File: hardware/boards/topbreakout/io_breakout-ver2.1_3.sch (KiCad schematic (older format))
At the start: 8 parts, among them J1 WURTH_ELECTRONICS_61400413321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, J2 MOLEX_52892-3033MOLEX_52892-3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, J3 USB-A-S-X-X-VT, J5 Conn_01x40

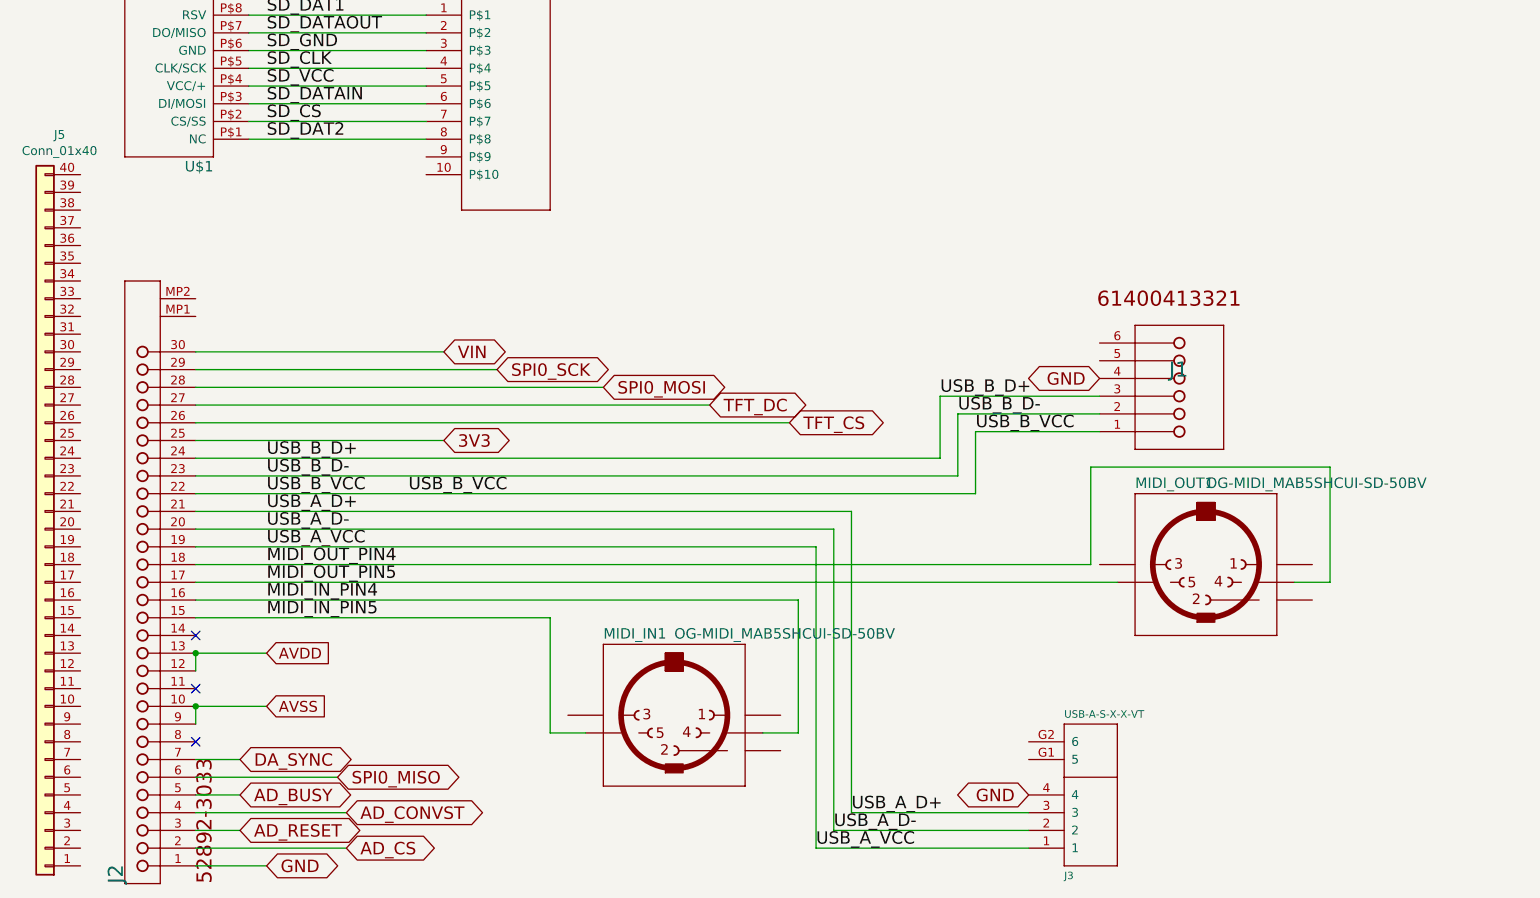
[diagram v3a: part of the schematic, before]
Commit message: moved midi circuit to breakout board
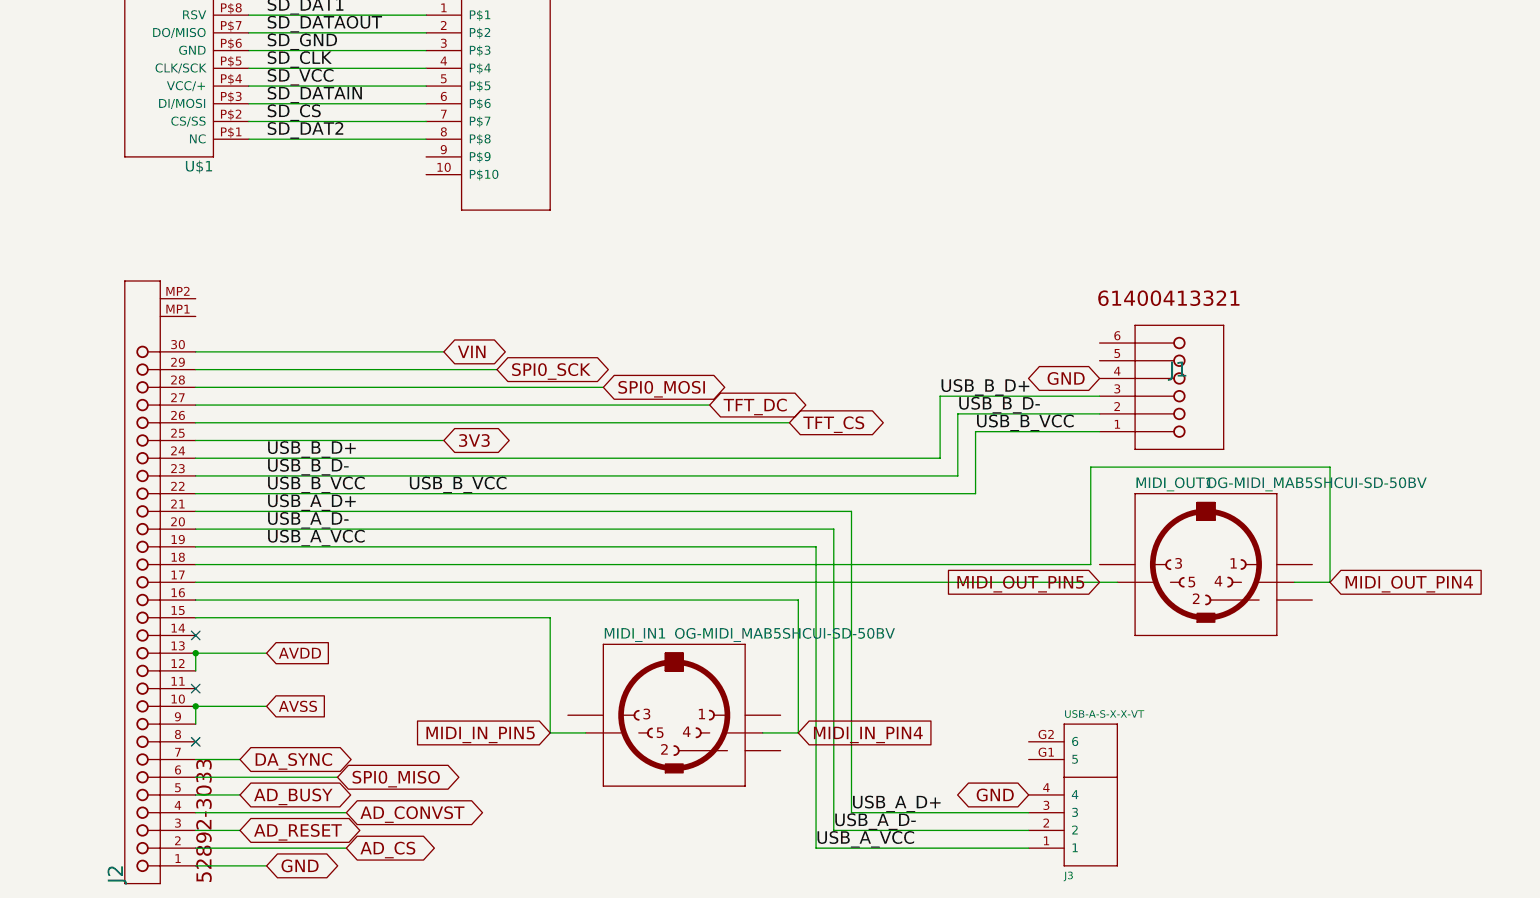
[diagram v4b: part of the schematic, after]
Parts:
- removed J5: Conn_01x40, Connectors_TE-Connectivity:TE_2-84953-7_1x27_P1.0mm_Horizontal, symbol Connector_Generic:Conn_01x40
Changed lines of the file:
@@
 $Descr User 14469 9224
 encoding utf-8
-Sheet 4 7
+Sheet 4 8
 Title ""
 Date ""
@@
 Wire Wire Line
 	1400 4600 3400 4600
-Text Label 1800 4600 0    70   ~ 0
-MIDI_IN_PIN5
-Text Label 1800 4500 0    70   ~ 0
-MIDI_IN_PIN4
-Text Label 1800 4400 0    70   ~ 0
-MIDI_OUT_PIN5
 Wire Wire Line
 	1400 4300 6450 4300
@@
 Wire Wire Line
 	6450 3750 7800 3750
-Text Label 1800 4300 0    70   ~ 0
-MIDI_OUT_PIN4
 Wire Wire Line
 	1400 4100 5000 4100
@@
 Text GLabel 1800 5100 2    61   Input ~ 0
 AVSS
-$Comp
-L Connector_Generic:Conn_01x40 J5
-U 1 1 5D8E7BFB
-P 550 4100
-F 0 "J5" H 468 1875 50  0000 C CNN
-F 1 "Conn_01x40" H 468 1966 50  0000 C CNN
-F 2 "Connectors_TE-Connectivity:TE_2-84953-7_1x27_P1.0mm_Horizontal" H 550 4100 50  0001 C CNN
-F 3 "~" H 550 4100 50  0001 C CNN
-	1    550  4100
-	-1   0    0    1
-$EndComp
+Text GLabel 7800 4400 2    70   Input ~ 0
+MIDI_OUT_PIN4
+Text GLabel 6500 4400 0    70   Input ~ 0
+MIDI_OUT_PIN5
+Text GLabel 4800 5250 2    70   Input ~ 0
+MIDI_IN_PIN4
+Text GLabel 3400 5250 0    70   Input ~ 0
+MIDI_IN_PIN5
 $EndSCHEMATC

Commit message: neaten up
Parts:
- removed MIDI_IN, MIDI_OUT: OG-MIDI_MAB5SHCUI-SD-50BV, topbreakout:OG-MIDI_SD-50BV, symbol TopBreakout-eagle-import:OG-MIDI_MAB5SHCUI-SD-50BV
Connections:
- net MIDI_IN_PIN4: no longer names the net of J2.16
- net MIDI_IN_PIN5: no longer names the net of J2.15
- net MIDI_OUT_PIN4 renamed MIDI_RX
- net MIDI_OUT_PIN5 renamed MIDI_TX
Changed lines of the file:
@@
 VIN
-Wire Wire Line
-	1400 4600 3400 4600
-Wire Wire Line
-	1400 4300 6450 4300
-Wire Wire Line
-	6450 4300 6450 3750
-Wire Wire Line
-	6450 3750 7800 3750
 Wire Wire Line
 	1400 4100 5000 4100
@@
 $EndComp
 $Comp
-L TopBreakout-eagle-import:OG-MIDI_MAB5SHCUI-SD-50BV MIDI_OUT
-U 1 1 74EA5AF5
-P 7100 4300
-AR Path="/74EA5AF5" Ref="MIDI_OUT"  Part="1"
-AR Path="/5D7F42FA/74EA5AF5" Ref="MIDI_OUT1"  Part="1"
-F 0 "MIDI_OUT1" H 6700 4725 59  0000 L BNN
-F 1 "OG-MIDI_MAB5SHCUI-SD-50BV" H 7100 4725 59  0000 L BNN
-F 2 "topbreakout:OG-MIDI_SD-50BV" H 7100 4300 50  0001 C CNN
-F 3 "" H 7100 4300 50  0001 C CNN
-	1    7100 4300
-	1    0    0    -1
-$EndComp
-$Comp
 L TopBreakout-eagle-import:MOLEX_52892-3033MOLEX_52892-3033_0_0 J2
 U 1 1 F1780596
@@
 $EndComp
 Wire Wire Line
-	3400 4600 3400 5250
-Wire Wire Line
 	6100 5900 4900 5900
-$Comp
-L TopBreakout-eagle-import:OG-MIDI_MAB5SHCUI-SD-50BV MIDI_IN
-U 1 1 1C421DBC
-P 4100 5150
-AR Path="/1C421DBC" Ref="MIDI_IN"  Part="1"
-AR Path="/5D7F42FA/1C421DBC" Ref="MIDI_IN1"  Part="1"
-F 0 "MIDI_IN1" H 3700 5575 59  0000 L BNN
-F 1 "OG-MIDI_MAB5SHCUI-SD-50BV" H 4100 5575 59  0000 L BNN
-F 2 "topbreakout:OG-MIDI_SD-50BV" H 4100 5150 50  0001 C CNN
-F 3 "" H 4100 5150 50  0001 C CNN
-	1    4100 5150
-	1    0    0    -1
-$EndComp
-Wire Wire Line
-	3400 5250 3600 5250
-Wire Wire Line
-	1400 4500 4800 4500
-Wire Wire Line
-	4600 5250 4800 5250
-Wire Wire Line
-	4800 5250 4800 4500
-Wire Wire Line
-	7600 4400 7800 4400
-Wire Wire Line
-	7800 4400 7800 3750
-Wire Wire Line
-	1400 4400 6600 4400
 Wire Wire Line
 	5100 5700 6100 5700
@@
 Text GLabel 1800 5100 2    61   Input ~ 0
 AVSS
-Text GLabel 7800 4400 2    70   Input ~ 0
-MIDI_OUT_PIN4
-Text GLabel 6500 4400 0    70   Input ~ 0
-MIDI_OUT_PIN5
-Text GLabel 4800 5250 2    70   Input ~ 0
-MIDI_IN_PIN4
-Text GLabel 3400 5250 0    70   Input ~ 0
-MIDI_IN_PIN5
+Text GLabel 1400 4300 2    59   Input ~ 0
+MIDI_RX
+Text GLabel 1400 4400 2    59   Input ~ 0
+MIDI_TX
 $EndSCHEMATC

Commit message: refactor
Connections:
- net AVDD: now also J2.10, J2.11; no longer J2.12, J2.13
- net AVSS: now also J2.8; no longer J2.10
- net GATE_2: now reaches J2.14
- net GATE_1: now reaches J2.15
- new net GATE_3: J2.13
- new net GATE_4: J2.12
- no-connect marks 3 -> 0
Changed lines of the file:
@@
-$EndComp
-$Comp
-L TopBreakout-eagle-import:MOLEX_52892-3033MOLEX_52892-3033_0_0 J2
-U 1 1 F1780596
-P 800 6100
-AR Path="/F1780596" Ref="J2"  Part="1"
-AR Path="/5D7F42FA/F1780596" Ref="J2"  Part="1"
-F 0 "J2" H 800 6000 85  0000 L TNN
-F 1 "MOLEX_52892-3033MOLEX_52892-3033_0_0" H 800 6100 50  0001 C CNN
-F 2 "topbreakout:MOLEX_52892-3033_0" H 800 6100 50  0001 C CNN
-F 3 "" H 800 6100 50  0001 C CNN
-	1    800  6100
-	0    -1   -1   0
 $EndComp
 $Comp
@@
 Wire Wire Line
 	5000 5800 6100 5800
-Wire Wire Line
-	1400 5200 1400 5100
-Wire Wire Line
-	1400 4900 1400 4800
-Wire Wire Line
-	1400 4800 1800 4800
-Connection ~ 1400 4800
-Wire Wire Line
-	1400 5100 1800 5100
-Connection ~ 1400 5100
-NoConn ~ 1400 5300
-NoConn ~ 1400 5000
-NoConn ~ 1400 4700
-Text GLabel 1800 4800 2    61   Input ~ 0
+Text GLabel 1800 5100 2    61   Input ~ 0
 AVDD
-Text GLabel 1800 5100 2    61   Input ~ 0
+Text GLabel 1800 5200 2    61   Input ~ 0
 AVSS
 Text GLabel 1400 4300 2    59   Input ~ 0
@@
 Text GLabel 1400 4400 2    59   Input ~ 0
 MIDI_TX
+$Comp
+L TopBreakout-eagle-import:MOLEX_52892-3033MOLEX_52892-3033_0_0 J2
+U 1 1 F1780596
+P 800 6100
+AR Path="/F1780596" Ref="J2"  Part="1"
+AR Path="/5D7F42FA/F1780596" Ref="J2"  Part="1"
+F 0 "J2" H 800 6000 85  0000 L TNN
+F 1 "MOLEX_52892-3033MOLEX_52892-3033_0_0" H 800 6100 50  0001 C CNN
+F 2 "topbreakout:MOLEX_52892-3033_0" H 800 6100 50  0001 C CNN
+F 3 "" H 800 6100 50  0001 C CNN
+	1    800  6100
+	0    -1   -1   0
+$EndComp
+Wire Wire Line
+	1400 5300 1400 5200
+Connection ~ 1400 5200
+Wire Wire Line
+	1400 5200 1800 5200
+Wire Wire Line
+	1800 5100 1400 5100
+Wire Wire Line
+	1400 5000 1400 5100
+Connection ~ 1400 5100
+Wire Wire Line
+	1400 4900 1600 4900
+Wire Wire Line
+	1400 4800 1600 4800
+Wire Wire Line
+	1400 4700 1600 4700
+Wire Wire Line
+	1400 4600 1600 4600
+Text GLabel 1600 4600 2    59   Input ~ 0
+GATE_1
+Text GLabel 1600 4700 2    59   Input ~ 0
+GATE_2
+Text GLabel 1600 4800 2    59   Input ~ 0
+GATE_3
+Text GLabel 1600 4900 2    59   Input ~ 0
+GATE_4
 $EndSCHEMATC

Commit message: routed, ERC checks success
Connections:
- net 3V3: now also J2.16, J2.17; no longer J2.25
- net AVDD: no longer J2.10
- net AVSS: now also J2.10; no longer J2.8, J2.9
- net DA_SYNC: now also J2.21; no longer J2.7
- net GND: now also J2.20
- net MIDI_RX: now also J2.24; no longer J2.18
- net MIDI_TX: now also J2.23; no longer J2.17
- net SPI0_MOSI: now also J2.22; no longer J2.28
- net SPI0_SCK: now also J2.7; no longer J2.29
- net TFT_CS: now also J2.8; no longer J2.26
- net TFT_DC: now also J2.9; no longer J2.27
- net USB_A_D+: now also J2.27; no longer J2.21
- net USB_A_D-: now also J2.26; no longer J2.20
- net USB_A_VCC: now also J2.25; no longer J2.19
- net USB_B_D+: now also J2.30; no longer J2.24
- net USB_B_D-: now also J2.29; no longer J2.23
- net USB_B_VCC: now also J2.28; no longer J2.22
- net VIN: now also J2.18, J2.19; no longer J2.30
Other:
- moved on the sheet: J1, J3
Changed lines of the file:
@@
 Comment4 ""
 $EndDescr
-Wire Wire Line
-	6500 3550 5800 3550
-Wire Wire Line
-	5800 3550 5800 3900
-Wire Wire Line
-	5800 3900 1400 3900
-Text Label 5800 3550 0    70   ~ 0
+Text Label 1800 3300 0    70   ~ 0
 USB_B_VCC
-Text Label 2600 3900 0    70   ~ 0
-USB_B_VCC
-Text Label 1800 3900 0    70   ~ 0
-USB_B_VCC
-Wire Wire Line
-	6500 3450 5700 3450
-Wire Wire Line
-	5700 3450 5700 3800
-Wire Wire Line
-	5700 3800 1400 3800
-Text Label 5700 3450 0    70   ~ 0
+Text Label 1700 3200 0    70   ~ 0
 USB_B_D-
-Text Label 1800 3800 0    70   ~ 0
-USB_B_D-
-Wire Wire Line
-	6500 3350 5600 3350
-Wire Wire Line
-	5600 3350 5600 3700
-Wire Wire Line
-	5600 3700 1400 3700
-Text Label 5600 3350 0    70   ~ 0
+Text Label 1600 3100 0    70   ~ 0
 USB_B_D+
-Text Label 1800 3700 0    70   ~ 0
-USB_B_D+
-Text GLabel 6100 5600 0    70   BiDi ~ 0
-GND
-Text GLabel 6500 3250 0    70   BiDi ~ 0
+Text GLabel 4600 3000 0    70   BiDi ~ 0
+GND
+Text GLabel 2150 2800 0    70   BiDi ~ 0
 GND
 Wire Wire Line
 	1400 6000 1800 6000
-Text GLabel 1800 6000 2    70   BiDi ~ 0
-GND
-Wire Wire Line
-	4900 5900 4900 4200
-Wire Wire Line
-	4900 4200 1400 4200
-Text Label 4900 5900 0    70   ~ 0
+Text GLabel 1400 4100 2    70   BiDi ~ 0
+GND
+Text Label 3550 3600 0    70   ~ 0
 USB_A_VCC
-Text Label 1800 4200 0    70   ~ 0
-USB_A_VCC
-Wire Wire Line
-	5100 5700 5100 4000
-Wire Wire Line
-	5100 4000 1400 4000
-Text Label 5100 5700 0    70   ~ 0
+Text Label 3750 3400 0    70   ~ 0
 USB_A_D+
-Text Label 1800 4000 0    70   ~ 0
-USB_A_D+
-Wire Wire Line
-	1400 3500 4750 3500
-Text GLabel 4750 3500 2    70   BiDi ~ 0
+Text GLabel 2350 5300 2    70   BiDi ~ 0
 TFT_CS
-Wire Wire Line
-	1400 3400 4300 3400
-Text GLabel 4300 3400 2    70   BiDi ~ 0
+Text GLabel 1800 5200 2    70   BiDi ~ 0
 TFT_DC
-Wire Wire Line
-	1400 3200 3100 3200
-Text GLabel 3100 3200 2    70   BiDi ~ 0
+Text GLabel 1650 5400 2    70   BiDi ~ 0
 SPI0_SCK
-Wire Wire Line
-	1400 3300 3700 3300
-Text GLabel 3700 3300 2    70   BiDi ~ 0
+Text GLabel 4450 4000 2    70   BiDi ~ 0
 SPI0_MOSI
 Wire Wire Line
-	1400 3100 2800 3100
-Text GLabel 2800 3100 2    70   BiDi ~ 0
+	2150 3800 3550 3800
+Text GLabel 1750 4200 2    70   BiDi ~ 0
 VIN
-Wire Wire Line
-	1400 4100 5000 4100
-Wire Wire Line
-	5000 4100 5000 5800
-Text Label 5000 5800 0    70   ~ 0
-USB_A_D-
-Text Label 1800 4100 0    70   ~ 0
+Text Label 3650 3500 0    70   ~ 0
 USB_A_D-
 Wire Wire Line
@@
 Wire Wire Line
 	1400 5400 1650 5400
-Text GLabel 1650 5400 2    70   BiDi ~ 0
+Text GLabel 5050 4100 2    70   BiDi ~ 0
 DA_SYNC
-Wire Wire Line
-	1400 3600 2800 3600
-Text GLabel 2800 3600 2    70   BiDi ~ 0
+Text GLabel 1600 4500 2    70   BiDi ~ 0
 3V3
 $Comp
 L TopBreakout-eagle-import:WURTH_ELECTRONICS_61400413321WURTH_ELECTRONICS_61400413321_0_0 J1
 U 1 1 92202B0B
-P 7100 3350
+P 3100 3100
 AR Path="/92202B0B" Ref="J1"  Part="1"
 AR Path="/5D7F42FA/92202B0B" Ref="J1"  Part="1"
-F 0 "J1" H 7200 3250 85  0000 L TNN
-F 1 "WURTH_ELECTRONICS_61400413321WURTH_ELECTRONICS_61400413321_0_0" H 7100 3350 50  0001 C CNN
-F 2 "topbreakout:WURTH_ELECTRONICS_61400413321_0" H 7100 3350 50  0001 C CNN
-F 3 "" H 7100 3350 50  0001 C CNN
-	1    7100 3350
+F 0 "J1" H 3200 3000 85  0000 L TNN
+F 1 "WURTH_ELECTRONICS_61400413321WURTH_ELECTRONICS_61400413321_0_0" H 3100 3100 50  0001 C CNN
+F 2 "topbreakout:WURTH_ELECTRONICS_61400413321_0" H 3100 3100 50  0001 C CNN
+F 3 "" H 3100 3100 50  0001 C CNN
+	1    3100 3100
 	-1   0    0    1
 $EndComp
@@
 L TopBreakout-eagle-import:USB-A-S-X-X-VT J3
 U 1 1 83A3164B
-P 6100 5900
+P 4750 3600
 AR Path="/83A3164B" Ref="J3"  Part="1"
 AR Path="/5D7F42FA/83A3164B" Ref="J3"  Part="1"
-F 0 "J3" H 6300 6031 42  0000 L BNN
-F 1 "USB-A-S-X-X-VT" H 6300 5120 42  0000 L BNN
-F 2 "topbreakout:USB-A-S-X-X-VT" H 6100 5900 50  0001 C CNN
-F 3 "" H 6100 5900 50  0001 C CNN
-	1    6100 5900
+F 0 "J3" H 4950 3731 42  0000 L BNN
+F 1 "USB-A-S-X-X-VT" H 4950 2820 42  0000 L BNN
+F 2 "topbreakout:USB-A-S-X-X-VT" H 4750 3600 50  0001 C CNN
+F 3 "" H 4750 3600 50  0001 C CNN
+	1    4750 3600
 	1    0    0    1
 $EndComp
@@
 	-1   0    0    -1
 $EndComp
-Wire Wire Line
-	6100 5900 4900 5900
-Wire Wire Line
-	5100 5700 6100 5700
-Wire Wire Line
-	5000 5800 6100 5800
-Text GLabel 1800 5100 2    61   Input ~ 0
+Text GLabel 2350 5000 2    61   Input ~ 0
 AVDD
-Text GLabel 1800 5200 2    61   Input ~ 0
+Text GLabel 2350 5100 2    61   Input ~ 0
 AVSS
-Text GLabel 1400 4300 2    59   Input ~ 0
+Text GLabel 3550 3800 2    59   Input ~ 0
 MIDI_RX
-Text GLabel 1400 4400 2    59   Input ~ 0
+Text GLabel 3850 3900 2    59   Input ~ 0
 MIDI_TX
 $Comp
@@
 $EndComp
 Wire Wire Line
-	1400 5300 1400 5200
-Connection ~ 1400 5200
-Wire Wire Line
 	1400 5200 1800 5200
-Wire Wire Line
-	1800 5100 1400 5100
-Wire Wire Line
-	1400 5000 1400 5100
-Connection ~ 1400 5100
 Wire Wire Line
 	1400 4900 1600 4900
@@
 Text GLabel 1600 4900 2    59   Input ~ 0
 GATE_4
+Wire Wire Line
+	2350 5300 1400 5300
+Wire Wire Line
+	4600 3000 4600 3300
+Wire Wire Line
+	4600 3300 4750 3300
+Wire Wire Line
+	2500 3000 2300 3000
+Wire Wire Line
+	2300 3000 2300 2800
+Wire Wire Line
+	2300 2800 2150 2800
+Wire Wire Line
+	1400 5000 2350 5000
+Wire Wire Line
+	1400 5100 2350 5100
+Text GLabel 1800 6000 2    70   BiDi ~ 0
+GND
+Wire Wire Line
+	1400 4500 1600 4500
+Wire Wire Line
+	1600 4400 1400 4400
+Wire Wire Line
+	1400 3300 2500 3300
+Wire Wire Line
+	1400 3200 2500 3200
+Wire Wire Line
+	1400 3100 2500 3100
+Wire Wire Line
+	3250 3400 3250 3500
+Wire Wire Line
+	3250 3500 2650 3500
+Wire Wire Line
+	2650 3500 2650 3400
+Wire Wire Line
+	2650 3400 1400 3400
+Wire Wire Line
+	3350 3500 3350 3600
+Wire Wire Line
+	3350 3600 2550 3600
+Wire Wire Line
+	2550 3600 2550 3500
+Wire Wire Line
+	2550 3500 1400 3500
+Wire Wire Line
+	3450 3600 3450 3700
+Wire Wire Line
+	3450 3700 2450 3700
+Wire Wire Line
+	2450 3700 2450 3600
+Wire Wire Line
+	2450 3600 1400 3600
+Wire Wire Line
+	3450 3600 4750 3600
+Wire Wire Line
+	3350 3500 4750 3500
+Wire Wire Line
+	3250 3400 4750 3400
+Wire Wire Line
+	2150 3800 2150 3700
+Wire Wire Line
+	2150 3700 1400 3700
+Wire Wire Line
+	2050 3900 2050 3800
+Wire Wire Line
+	2050 3800 1400 3800
+Wire Wire Line
+	2050 3900 3850 3900
+Wire Wire Line
+	1950 4000 1950 3900
+Wire Wire Line
+	1950 3900 1400 3900
+Wire Wire Line
+	1950 4000 4450 4000
+Wire Wire Line
+	1850 4100 1850 4000
+Wire Wire Line
+	1850 4000 1400 4000
+Wire Wire Line
+	1850 4100 5050 4100
+Wire Wire Line
+	1400 4200 1750 4200
+Wire Wire Line
+	1400 4300 2000 4300
+Text GLabel 2000 4300 2    70   BiDi ~ 0
+VIN
+Text GLabel 1600 4400 2    70   BiDi ~ 0
+3V3
 $EndSCHEMATC

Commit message: revision 1.4 changes
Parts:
- U$2: footprint topbreakout:TE_1-1734592-8 -> common:HFW8R-1STE1LF
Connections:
- net 3V3 renamed +3V3
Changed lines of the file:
@@
-EESchema Schematic File Version 4
-LIBS:TopBreakout-cache
+EESchema Schematic File Version 5
 EELAYER 30 0
 EELAYER END
@@
 Comment3 ""
 Comment4 ""
+Comment5 ""
+Comment6 ""
+Comment7 ""
+Comment8 ""
+Comment9 ""
 $EndDescr
 Text Label 1800 3300 0    70   ~ 0
@@
 DA_SYNC
 Text GLabel 1600 4500 2    70   BiDi ~ 0
-3V3
++3V3
 $Comp
 L TopBreakout-eagle-import:WURTH_ELECTRONICS_61400413321WURTH_ELECTRONICS_61400413321_0_0 J1
@@
 F 0 "U$2" H 2200 1800 50  0001 C CNN
 F 1 "1734592-8" H 2200 1800 50  0001 C CNN
-F 2 "topbreakout:TE_1-1734592-8" H 2200 1800 50  0001 C CNN
+F 2 "common:HFW8R-1STE1LF" H 2200 1800 50  0001 C CNN
 F 3 "" H 2200 1800 50  0001 C CNN
 	1    2200 1800
@@
 VIN
 Text GLabel 1600 4400 2    70   BiDi ~ 0
-3V3
++3V3
 $EndSCHEMATC
